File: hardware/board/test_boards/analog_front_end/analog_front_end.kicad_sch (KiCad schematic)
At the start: 23 parts, among them J5 Barrel_Jack_Switch, U5 LT3030, U6 LM27762

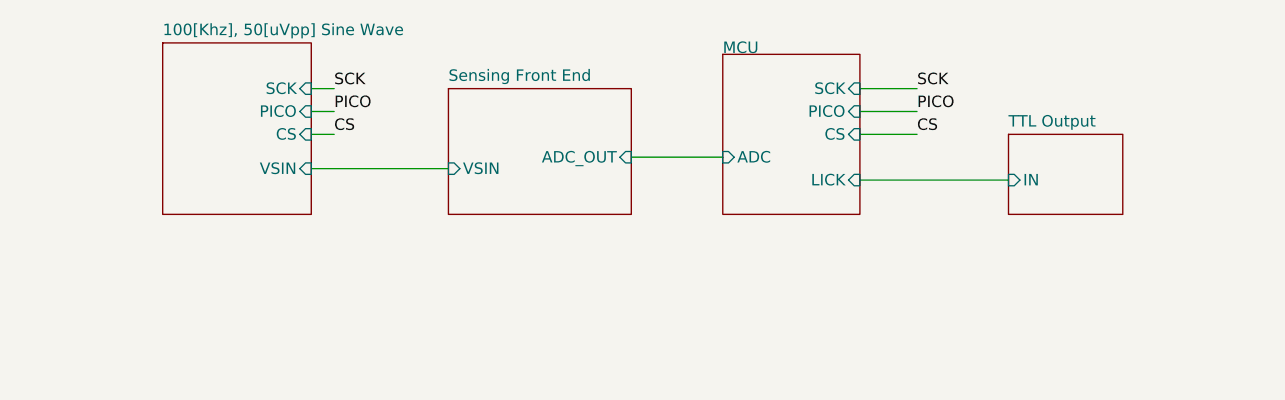
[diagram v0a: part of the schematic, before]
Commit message: add analog front end test board
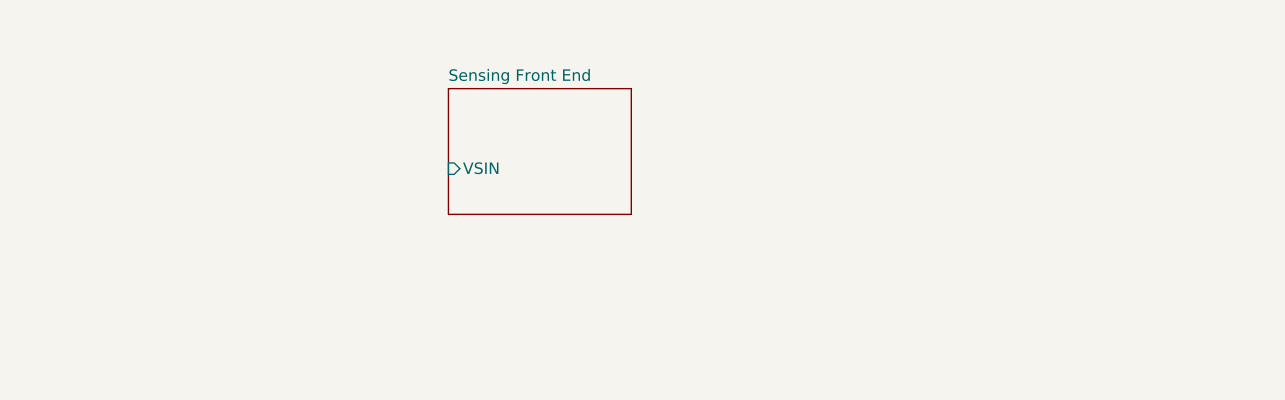
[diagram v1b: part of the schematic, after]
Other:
- removed sheet 100[Khz], 50[uVpp] Sine Wave
- removed sheet MCU
- removed sheet TTL Output
- sheet Sensing Front End ports: added none; removed ADC_OUT

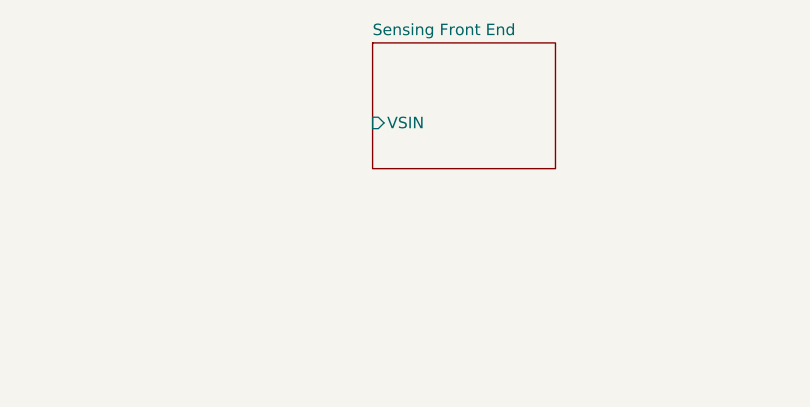
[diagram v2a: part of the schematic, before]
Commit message: finish first draft of analog front end pcb
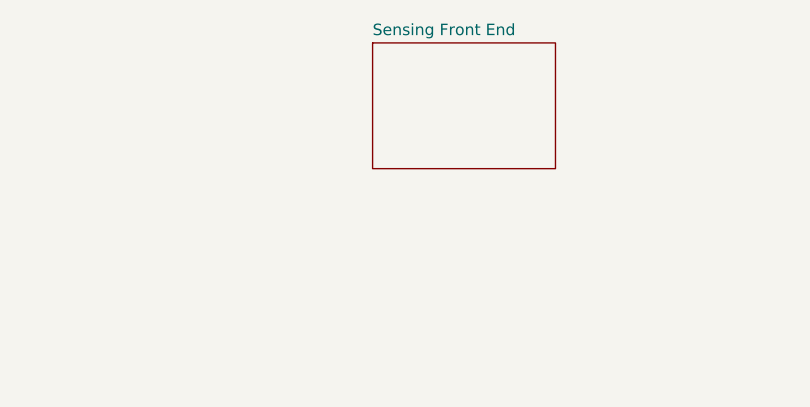
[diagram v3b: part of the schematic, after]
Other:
- sheet Sensing Front End ports: added none; removed VSIN
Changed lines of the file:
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@@
       (effects (font (size 1.27 1.27)) (justify left top) hide)
-    )
-    (pin "VSIN" input (at 119.38 71.12 180)
-      (effects (font (size 1.27 1.27)) (justify left))
     )
   )

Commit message: update analog frontend bom
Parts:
- C1: value 3.3uF -> (none); footprint Capacitor_SMD:C_0805_2012Metric_Pad1.18x1.45mm_HandSolder -> (none)
- C2, C3: value 10nF -> (none); footprint Capacitor_SMD:C_0603_1608Metric_Pad1.08x0.95mm_HandSolder -> (none)
- C4: value 10uF -> (none); footprint Capacitor_SMD:C_0805_2012Metric -> (none)
- C5: value 22uF -> (none); footprint Capacitor_SMD:C_0805_2012Metric -> (none)
- C6: value 1uF -> (none); footprint Capacitor_SMD:C_0603_1608Metric_Pad1.08x0.95mm_HandSolder -> (none)
- C7: value 4.7uF -> (none); footprint Capacitor_SMD:C_0805_2012Metric_Pad1.18x1.45mm_HandSolder -> (none)
- C8, C9: value 2.2uF -> (none); footprint Capacitor_SMD:C_0603_1608Metric_Pad1.08x0.95mm_HandSolder -> (none); Link https://www.digikey.com/en/products/detail/murata-electronics/GRM188Z71E225KE43D/16602147 -> https://www.digikey.com/en/products/detail/murata-electronics/GRM188C71E225KE11D/5797701; Manufacturer Number GRM188Z71E225KE43D -> GRM188C71E225KE11D; Temperature Coefficient X7R -> X7S
- J5: value Barrel_Jack_Switch -> (none); footprint Connector_BarrelJack:BarrelJack_CUI_PJ-036AH-SMT_Horizontal -> (none)
- R1, R2: value 1M -> (none); footprint Resistor_SMD:R_0603_1608Metric_Pad0.98x0.95mm_HandSolder -> (none)
- R11: value 54K9 -> (none); footprint Resistor_SMD:R_0603_1608Metric_Pad0.98x0.95mm_HandSolder -> (none)
- R12, R14: value 51K -> (none); footprint Resistor_SMD:R_0603_1608Metric_Pad0.98x0.95mm_HandSolder -> (none)
- R13: value 53K6 -> (none); footprint Resistor_SMD:R_0603_1608Metric_Pad0.98x0.95mm_HandSolder -> (none)
- R3: value 10K -> (none); footprint Resistor_SMD:R_0402_1005Metric_Pad0.72x0.64mm_HandSolder -> (none)
- R51, R61: value 100K -> (none); footprint Resistor_SMD:R_0603_1608Metric_Pad0.98x0.95mm_HandSolder -> (none)
- R52: value 309K -> (none); footprint Resistor_SMD:R_0603_1608Metric_Pad0.98x0.95mm_HandSolder -> (none)
- R62: value 172K -> (none); footprint Resistor_SMD:R_0603_1608Metric_Pad0.98x0.95mm_HandSolder -> (none)
- U5: value LT3030 -> (none); footprint Package_SO:ETSSOP-20-1EP_4.4x6.5mm_P0.65mm_EP3x4.2mm -> (none)
- U6: value LM27762 -> (none); footprint Package_SON:WSON-12-1EP_3x2mm_P0.5mm_EP1x2.65_ThermalVias -> (none); Link (none) -> https://www.digikey.com/en/products/detail/texas-instrument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

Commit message: get sine wave chip output working
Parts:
- C1: value (none) -> 3.3uF; footprint (none) -> Capacitor_SMD:C_0805_2012Metric_Pad1.18x1.45mm_HandSolder
- C2, C3: value (none) -> 10nF; footprint (none) -> Capacitor_SMD:C_0603_1608Metric_Pad1.08x0.95mm_HandSolder
- C4: value (none) -> 10uF; footprint (none) -> Capacitor_SMD:C_0805_2012Metric
- C5: value (none) -> 22uF; footprint (none) -> Capacitor_SMD:C_0805_2012Metric
- C6: value (none) -> 1uF; footprint (none) -> Capacitor_SMD:C_0603_1608Metric_Pad1.08x0.95mm_HandSolder
- C7: value (none) -> 4.7uF; footprint (none) -> Capacitor_SMD:C_0805_2012Metric_Pad1.18x1.45mm_HandSolder
- C8, C9: value (none) -> 2.2uF; footprint (none) -> Capacitor_SMD:C_0603_1608Metric_Pad1.08x0.95mm_HandSolder
- J5: value (none) -> Barrel_Jack_Switch; footprint (none) -> Connector_BarrelJack:BarrelJack_CUI_PJ-036AH-SMT_Horizontal
- R1, R2: value (none) -> 1M; footprint (none) -> Resistor_SMD:R_0603_1608Metric_Pad0.98x0.95mm_HandSolder
- R11: value (none) -> 54K9; footprint (none) -> Resistor_SMD:R_0603_1608Metric_Pad0.98x0.95mm_HandSolder
- R12, R14: value (none) -> 51K; footprint (none) -> Resistor_SMD:R_0603_1608Metric_Pad0.98x0.95mm_HandSolder
- R13: value (none) -> 53K6; footprint (none) -> Resistor_SMD:R_0603_1608Metric_Pad0.98x0.95mm_HandSolder
- R3: value (none) -> 10K; footprint (none) -> Resistor_SMD:R_0402_1005Metric_Pad0.72x0.64mm_HandSolder
- R51, R61: value (none) -> 100K; footprint (none) -> Resistor_SMD:R_0603_1608Metric_Pad0.98x0.95mm_HandSolder
- R52: value (none) -> 309K; footprint (none) -> Resistor_SMD:R_0603_1608Metric_Pad0.98x0.95mm_HandSolder
- R62: value (none) -> 172K; footprint (none) -> Resistor_SMD:R_0603_1608Metric_Pad0.98x0.95mm_HandSolder
- U5: value (none) -> LT3030; footprint (none) -> Package_SO:ETSSOP-20-1EP_4.4x6.5mm_P0.65mm_EP3x4.2mm
- U6: value (none) -> LM27762; footprint (none) -> Package_SON:WSON-12-1EP_3x2mm_P0.5mm_EP1x2.65_ThermalVias

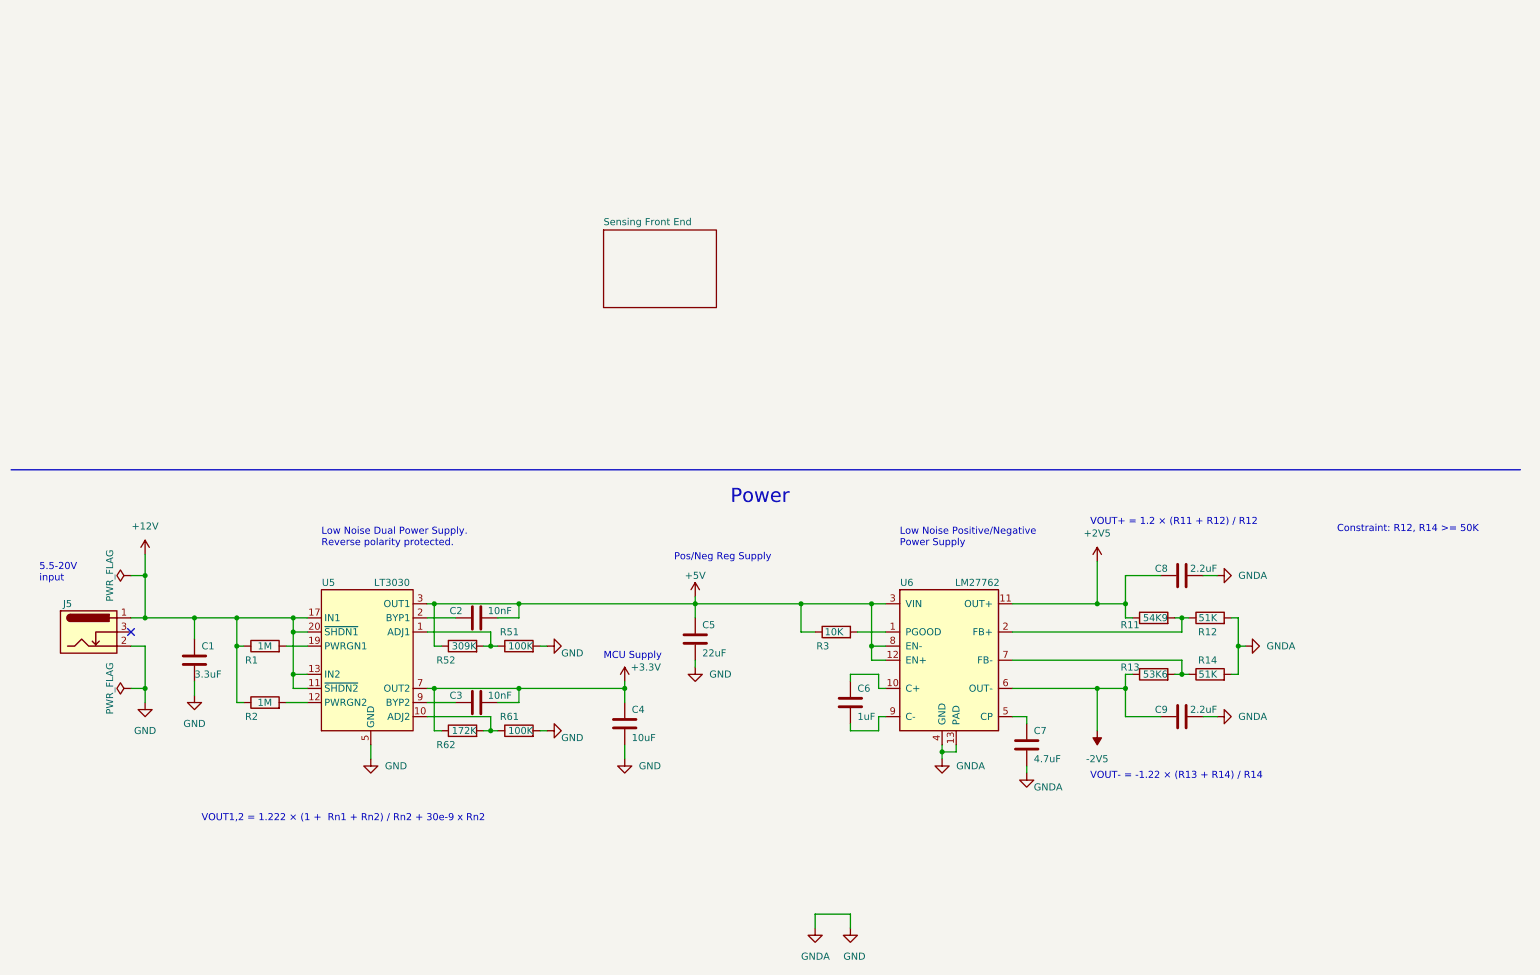
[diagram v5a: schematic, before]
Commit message: update bandpass filter; plan pico shield version
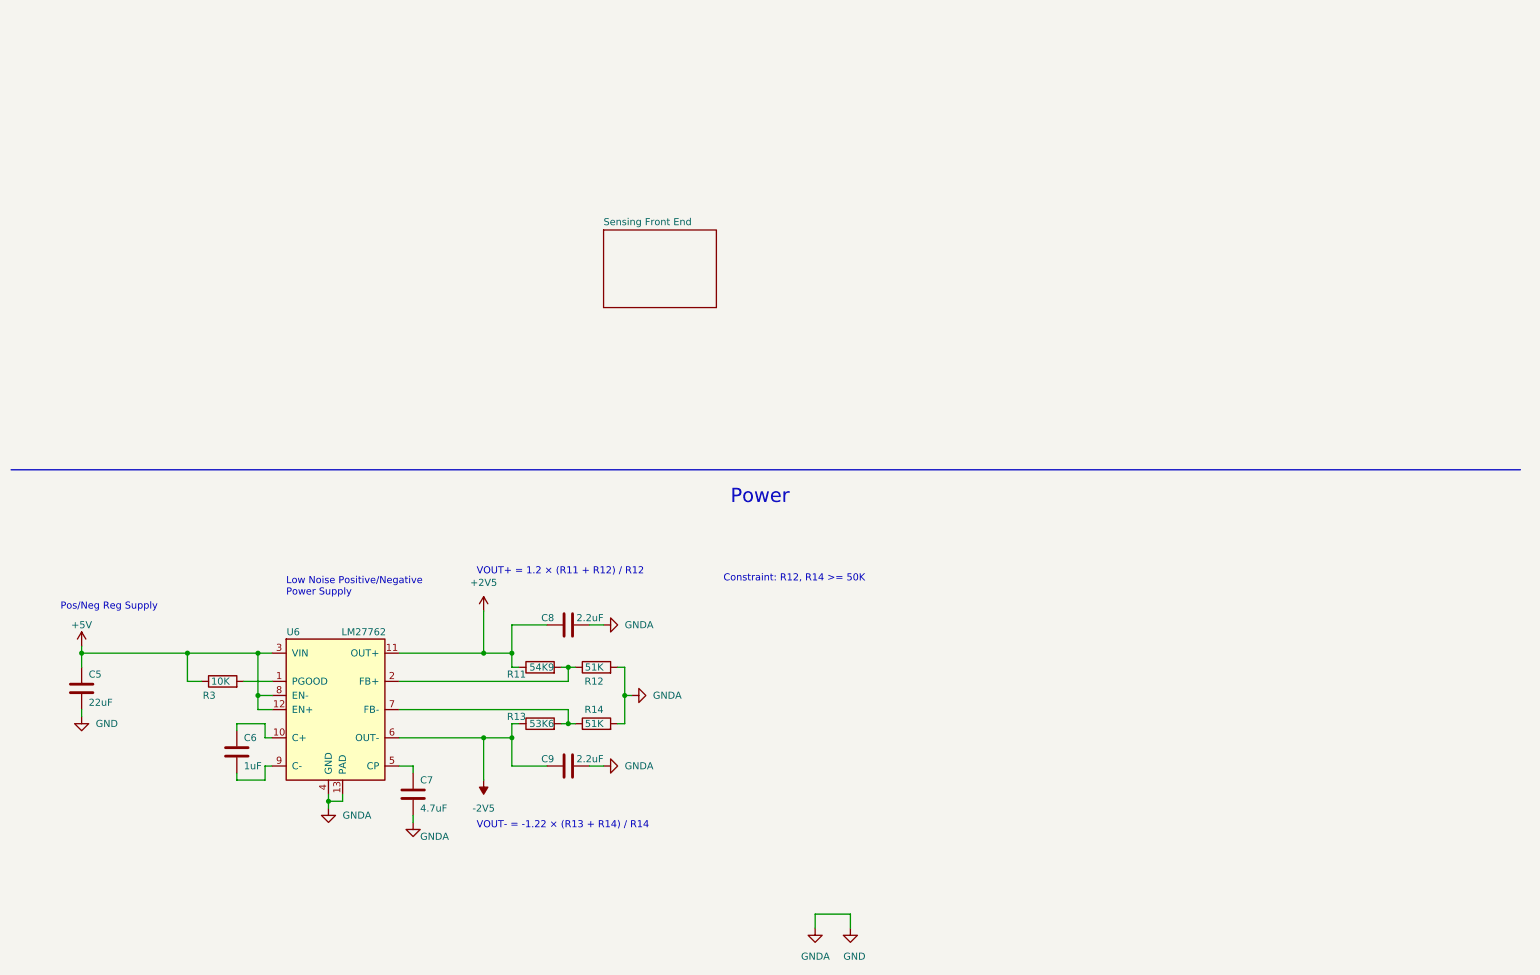
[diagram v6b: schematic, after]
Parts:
- removed C1: 3.3uF, Capacitor_SMD:C_0805_2012Metric_Pad1.18x1.45mm_HandSolder, symbol Device:C
- removed C2, C3: 10nF, Capacitor_SMD:C_0603_1608Metric_Pad1.08x0.95mm_HandSolder, symbol Device:C
- removed C4: 10uF, Capacitor_SMD:C_0805_2012Metric, symbol Device:C
- removed J5: Barrel_Jack_Switch, Connector_BarrelJack:BarrelJack_CUI_PJ-036AH-SMT_Horizontal, symbol Connector:Barrel_Jack_Switch
- removed R1, R2: 1M, Resistor_SMD:R_0603_1608Metric_Pad0.98x0.95mm_HandSolder, symbol Device:R
- removed R51, R61: 100K, Resistor_SMD:R_0603_1608Metric_Pad0.98x0.95mm_HandSolder, symbol Device:R
- removed R52: 309K, Resistor_SMD:R_0603_1608Metric_Pad0.98x0.95mm_HandSolder, symbol Device:R
- removed R62: 172K, Resistor_SMD:R_0603_1608Metric_Pad0.98x0.95mm_HandSolder, symbol Device:R
- removed U5: LT3030, Package_SO:ETSSOP-20-1EP_4.4x6.5mm_P0.65mm_EP3x4.2mm, symbol machine_agency_components:LT3030
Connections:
- no-connect marks 1 -> 0
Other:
- note removed: "5.5-20V input"
- note removed: "Low Noise Dual Power Supply. Reverse polarity protected."
- note removed: "MCU Supply"
- note removed: "VOUT1,2 = 1.222 × (1 + Rn1 + Rn2) / Rn2 + 30e-9 x Rn2"
- moved on the sheet: C5, C6, C7, C8, C9, R11, R12, R13, R14, R3, U6

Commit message: ship rev2 of test pcbs
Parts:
- added J1, J2: Conn_01x20_Female, Connector_PinHeader_2.54mm:PinHeader_1x20_P2.54mm_Vertical, symbol Connector:Conn_01x20_Female
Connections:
- net +5V: now also J2.19 (Pin_19)
- net GND: now also J1.13 (Pin_13), J1.18 (Pin_18), J1.3 (Pin_3), J1.8 (Pin_8), J2.13 (Pin_13), J2.18 (Pin_18), J2.3 (Pin_3), J2.8 (Pin_8)
- new net +3V3: J2.16 (Pin_16)
- new net CS: J1.2 (Pin_2)
- new net PICO: J1.5 (Pin_5)
- new net SCK: J1.4 (Pin_4)
- new net VSIG: J2.11 (Pin_11)
- no-connect marks 0 -> 26
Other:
- added sheet 100KHz Sine Wave Source (sine_wave_source.kicad_sch)
- sheet Sensing Front End ports: added VSIG, VSINE; removed none
- note added: "21"
- note added: "22"
- note added: "Analog Power"
- note added: "GP1"
- note added: "GP2"
- note added: "GP26"
- note added: "GP3"
- note removed: "Power"
